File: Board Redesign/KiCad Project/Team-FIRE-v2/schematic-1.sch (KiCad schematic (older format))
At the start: 32 parts, among them J1 SIM_Card, J2 53885-0408, U1 TPS40210DGQR, U2 NCN4555MN, U3 CSD18543Q3A

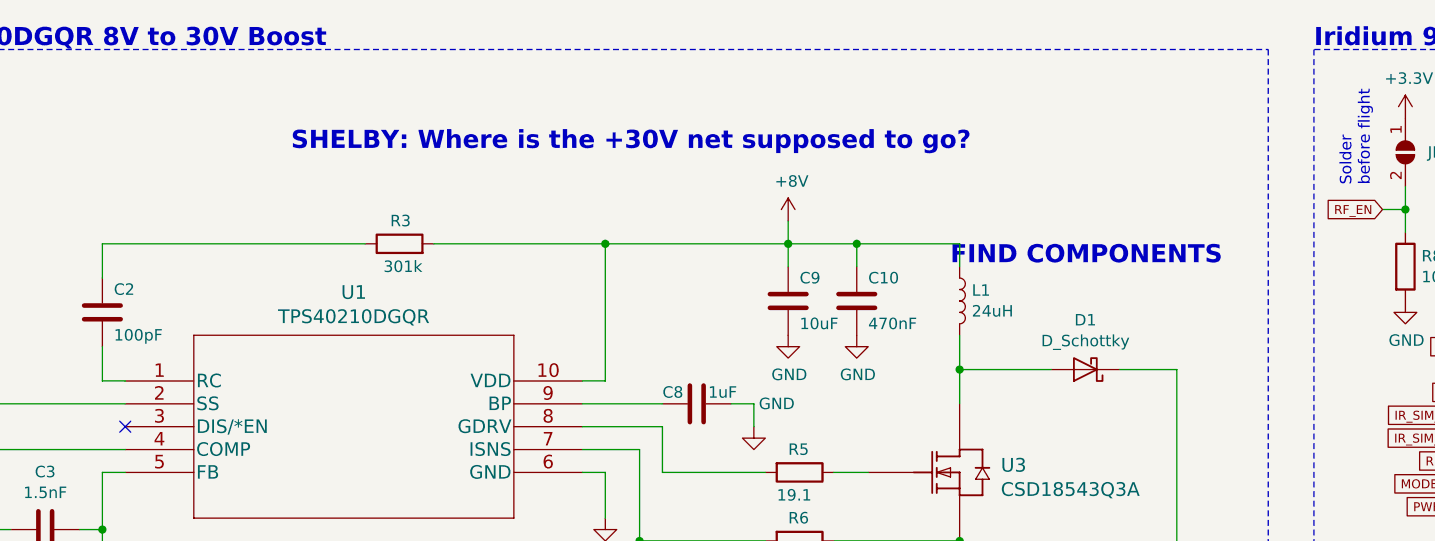
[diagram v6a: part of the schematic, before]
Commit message: 30V net for boost
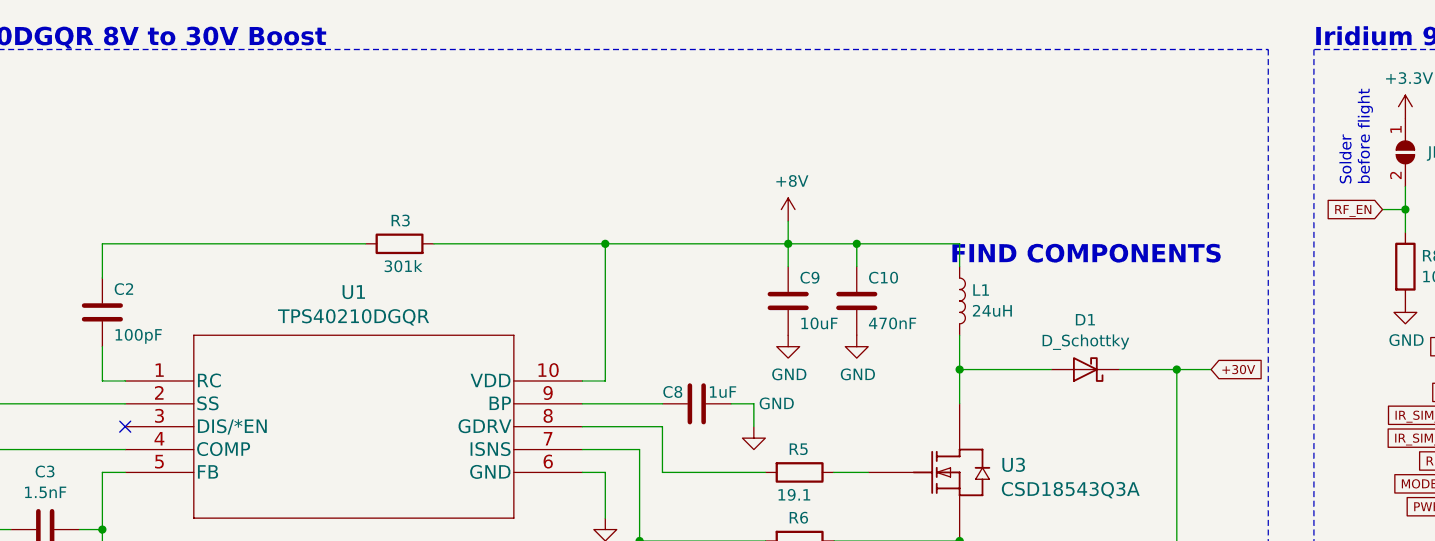
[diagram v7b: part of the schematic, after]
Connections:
- net +30V: now also C11.1 (+_1), C11.3 (+_2), C11.4 (+_3), C13.1, D1.1 (K), R4.2
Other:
- note removed: "SHELBY: Where is the +30V net supposed to go?"
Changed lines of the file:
@@
 EESchema Schematic File Version 4
-LIBS:Team-FIRE-v2-cache
 EELAYER 30 0
 EELAYER END
@@
 Wire Wire Line
 	1750 2100 1750 2250
-Text Notes 5550 1250 2    79   ~ 16
-SHELBY: Where is the +30V net supposed to go?
 Text Notes 8100 5850 0    79   ~ 16
 PART SELECTION FINISHED - COLLIN
 Text Notes 7900 950  0    79   ~ 16
 PART SELECTION FINISHED - COLLIN
+Text GLabel 6600 2200 2    39   Input ~ 0
++30V
+Wire Wire Line
+	6600 2200 6450 2200
+Connection ~ 6450 2200
 $EndSCHEMATC
